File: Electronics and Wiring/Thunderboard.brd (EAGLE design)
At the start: 84.1 x 54.6 mm, 33 parts, among them Q1 TIP120, Q2 TIP120, Q3 TIP120, T1 2n2222

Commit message: Updating electronics files
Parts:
- R9: value 1K -> 3K
- T1: value 2n2222 -> PN2222A
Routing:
- net GND: track 4.74 -> 4.21 mm
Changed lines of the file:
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@@
 <layer number="19" name="Unrouted" color="6" fill="1" visible="no" active="yes"/>
 <layer number="20" name="Dimension" color="24" fill="1" visible="yes" active="yes"/>
-<layer number="21" name="tPlace" color="7" fill="1" visible="no" active="yes"/>
+<layer number="21" name="tPlace" color="7" fill="1" visible="yes" active="yes"/>
 <layer number="22" name="bPlace" color="7" fill="1" visible="no" active="yes"/>
 <layer number="23" name="tOrigins" color="15" fill="1" visible="no" active="yes"/>
@@
 <attribute name="VALUE" x="50.038" y="24.765" size="0.6096" layer="27" font="vector" ratio="20" rot="R270" align="top-center"/>
 </element>
-<element name="T1" library="transistor" library_urn="urn:adsk.eagle:library:402" package="TO92-EBC" package3d_urn="urn:adsk.eagle:package:29915/2" value="2n2222" x="49.53" y="33.655" smashed="yes" rot="R270">
+<element name="T1" library="transistor" library_urn="urn:adsk.eagle:library:402" package="TO92-EBC" package3d_urn="urn:adsk.eagle:package:29915/2" value="PN2222A" x="49.53" y="33.655" smashed="yes" rot="R270">
 <attribute name="NAME" x="51.308" y="36.195" size="1.27" layer="25" ratio="10" rot="R270"/>
 </element>
-<element name="R9" library="resistor - edit" package="0207/7" package3d_urn="urn:adsk.eagle:package:25942/1" value="1K" x="47.625" y="42.545" smashed="yes" rot="R270">
+<element name="R9" library="resistor - edit" package="0207/7" package3d_urn="urn:adsk.eagle:package:25942/1" value="3K" x="47.625" y="42.545" smashed="yes" rot="R270">
 <attribute name="NAME" x="49.022" y="45.085" size="1.27" layer="25" ratio="10" rot="R270"/>
 <attribute name="VALUE" x="47.0662" y="44.831" size="1.27" layer="27" ratio="10" rot="R270"/>
@@
 <wire x1="7.62" y1="14.28" x2="7.62" y2="15.4305" width="0.508" layer="16"/>
 <wire x1="7.62" y1="15.4305" x2="9.2282" y2="15.4305" width="0.508" layer="16"/>
-<wire x1="9.59885" y1="15.80115" x2="9.2282" y2="15.4305" width="0.508" layer="16"/>
 <wire x1="7.62" y1="15.4305" x2="6.5405" y2="15.4305" width="0.508" layer="16"/>
 <wire x1="6.5405" y1="15.4305" x2="6.27615" y2="15.16615" width="0.508" layer="16"/>
@@
 <wire x1="27.432" y1="12.8997" x2="38.0793" y2="23.547" width="3.175" layer="16"/>
 <wire x1="45.17055" y1="23.547" x2="55.245" y2="33.62145" width="2.54" layer="16"/>
-<wire x1="55.245" y1="33.62145" x2="55.245" y2="34.925" width="2.54" layer="16"/>
+<wire x1="55.245" y1="33.62145" x2="55.245" y2="34.925" width="2.032" layer="16"/>
 </signal>
 <signal name="D11">

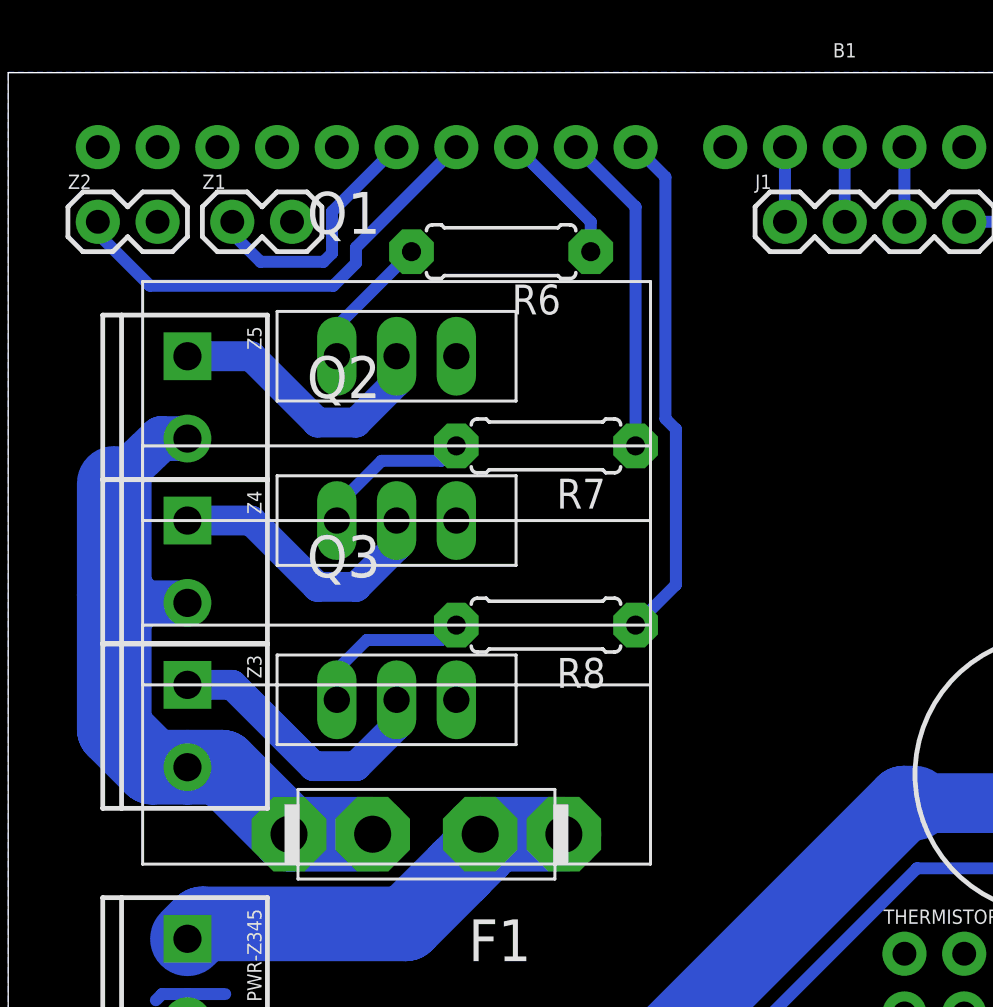
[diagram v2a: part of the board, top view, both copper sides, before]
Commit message: Changes made after testing the Thunderboard. Switched from Tip120 to a power fet STP55NF06L.
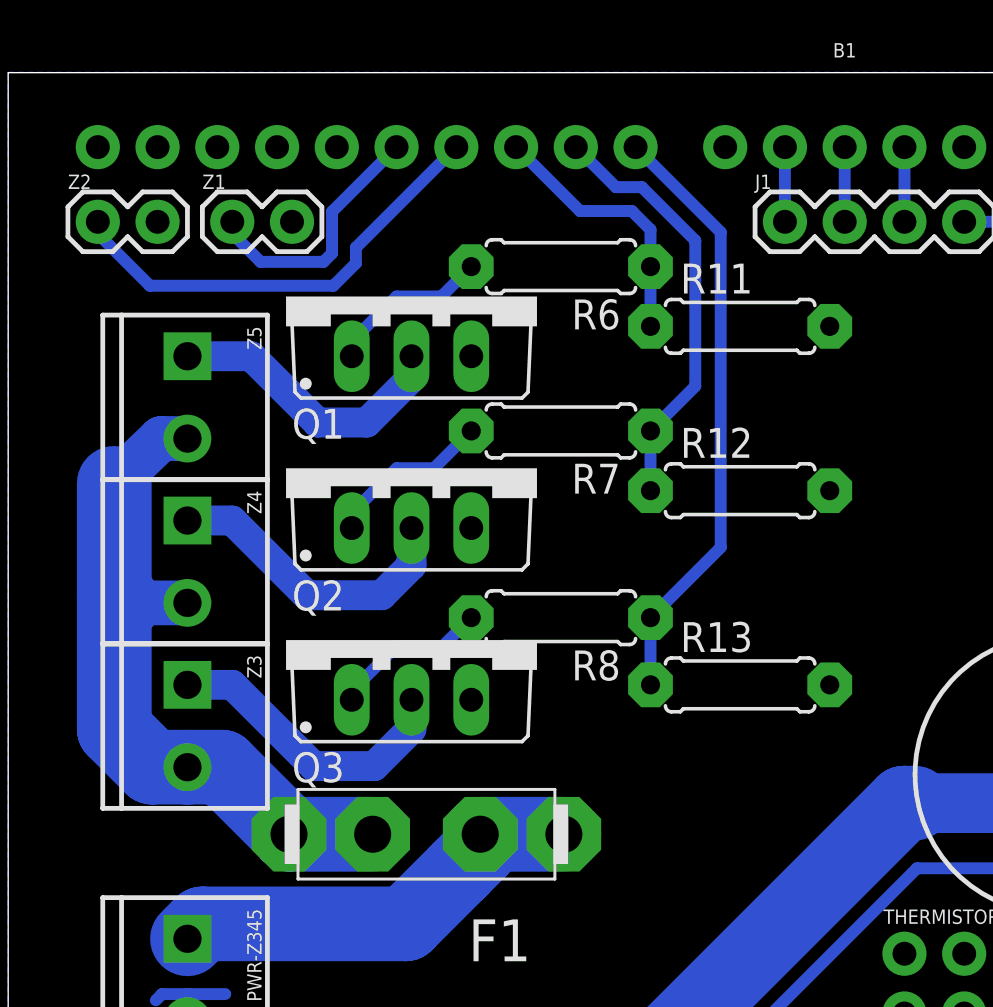
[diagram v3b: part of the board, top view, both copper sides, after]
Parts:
- added R11, R12, R13: 100k, resistor - edit:0207/7
- F1: value (none) -> 10 A
- F2: value (none) -> 5A
- Q1, Q2, Q3: value TIP120 -> STP55NF06L; device Edited Parts:TO220AH -> Edited Parts:TO-220
- R6, R7, R8: value 1K -> 100R
- moved R6 2.62 mm to (23.5, 46.4)
- moved Q1 2.62 mm to (17.1, 45.1)
- moved Q3 2.62 mm to (17.1, 30.5)
- moved Q2 2.31 mm to (17.1, 37.8)
- moved R7 0.90 mm to (23.5, 39.4)
- moved R8 0.71 mm to (23.5, 31.4)
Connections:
- net D10: now also R11.1
- net D8: now also R13.1
- net D9: now also R12.1
- net GND: now also Q1.S, Q2.S, Q3.S, R11.2, R12.2, R13.2; no longer Q1.E, Q2.E, Q3.E
- net N$10: now also Q3.D; no longer Q3.C
- net N$3: now also Q1.G; no longer Q1.B
- net N$4: now also Q2.G; no longer Q2.B
- net N$5: now also Q3.G; no longer Q3.B
- net N$7: now also Q1.D; no longer Q1.C
- net N$9: now also Q2.D; no longer Q2.C
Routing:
- net D10: track 5.76 -> 11.9 mm
- net D9: track 13.8 -> 18.1 mm
- net D8: track 21.7 -> 25.6 mm
- net N$3: track 5.76 -> 7.03 mm
- net N$9: track 11.9 -> 13.0 mm
- net N$10: track 12.1 -> 12.8 mm
- net N$7: track 11.9 -> 12.4 mm
